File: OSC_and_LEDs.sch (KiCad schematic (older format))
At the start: 56 parts, among them Q11 IRLML2502, Q12 IRLML2502, Q14 IRLML2502, Q15 IRLML2502, Q8 IRLML2502, Q9 IRLML2502, U1 xc7a50tftg256, X1 ASFLMB

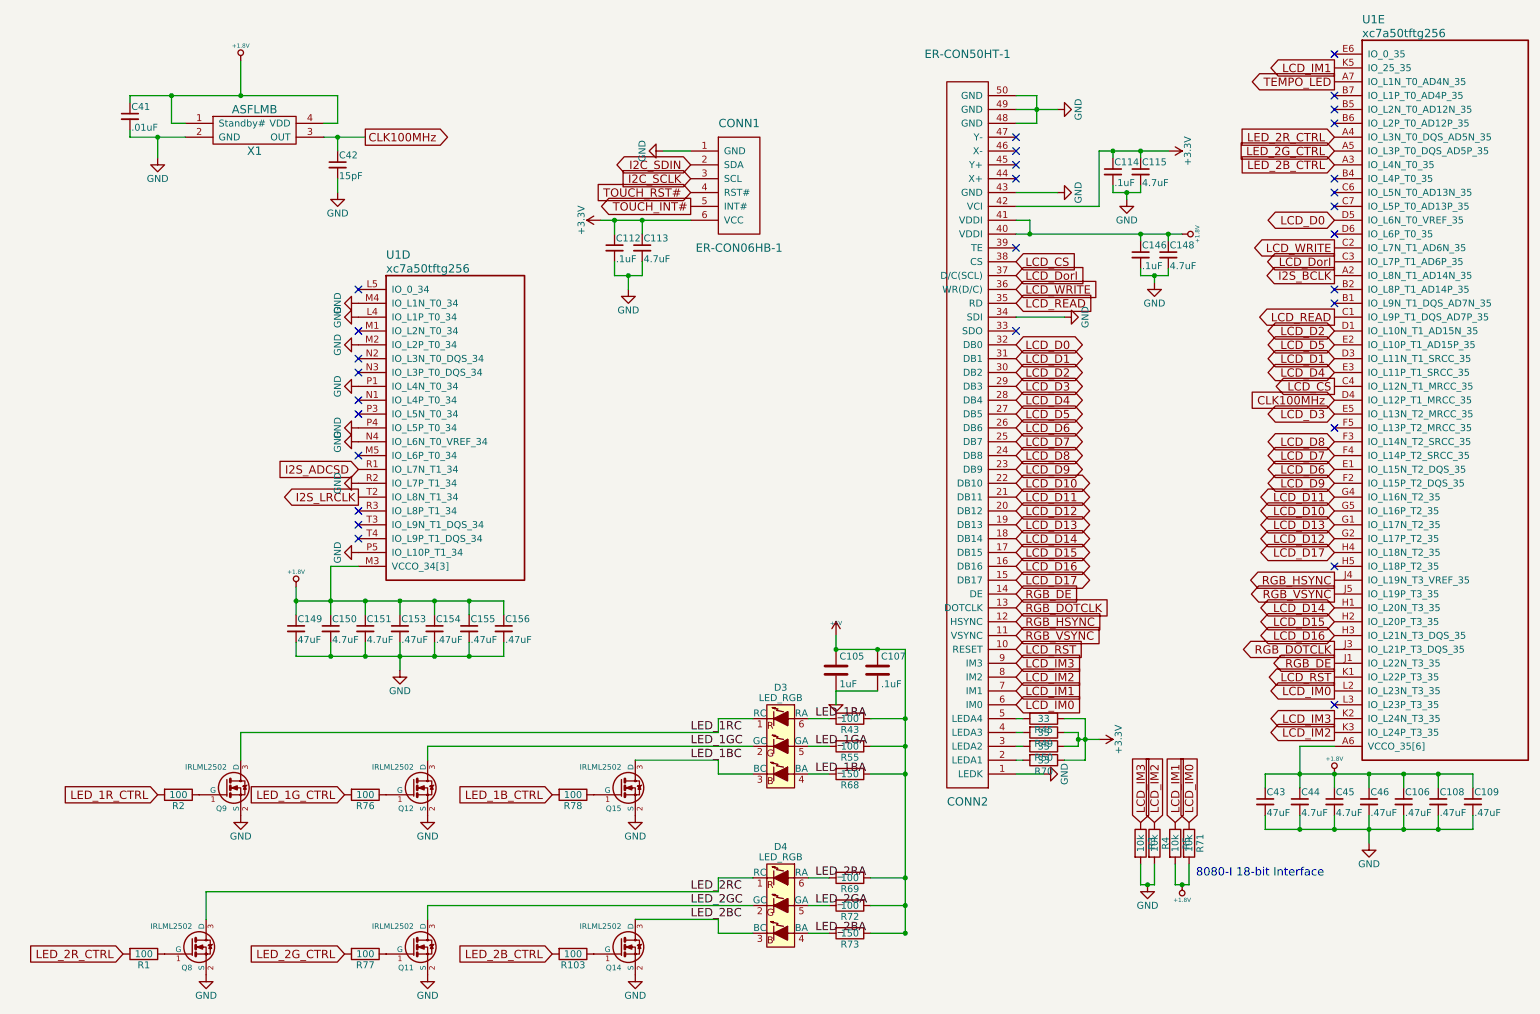
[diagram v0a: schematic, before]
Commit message: added and length-matched DDR2 ram, compliant to Xilinx MIG
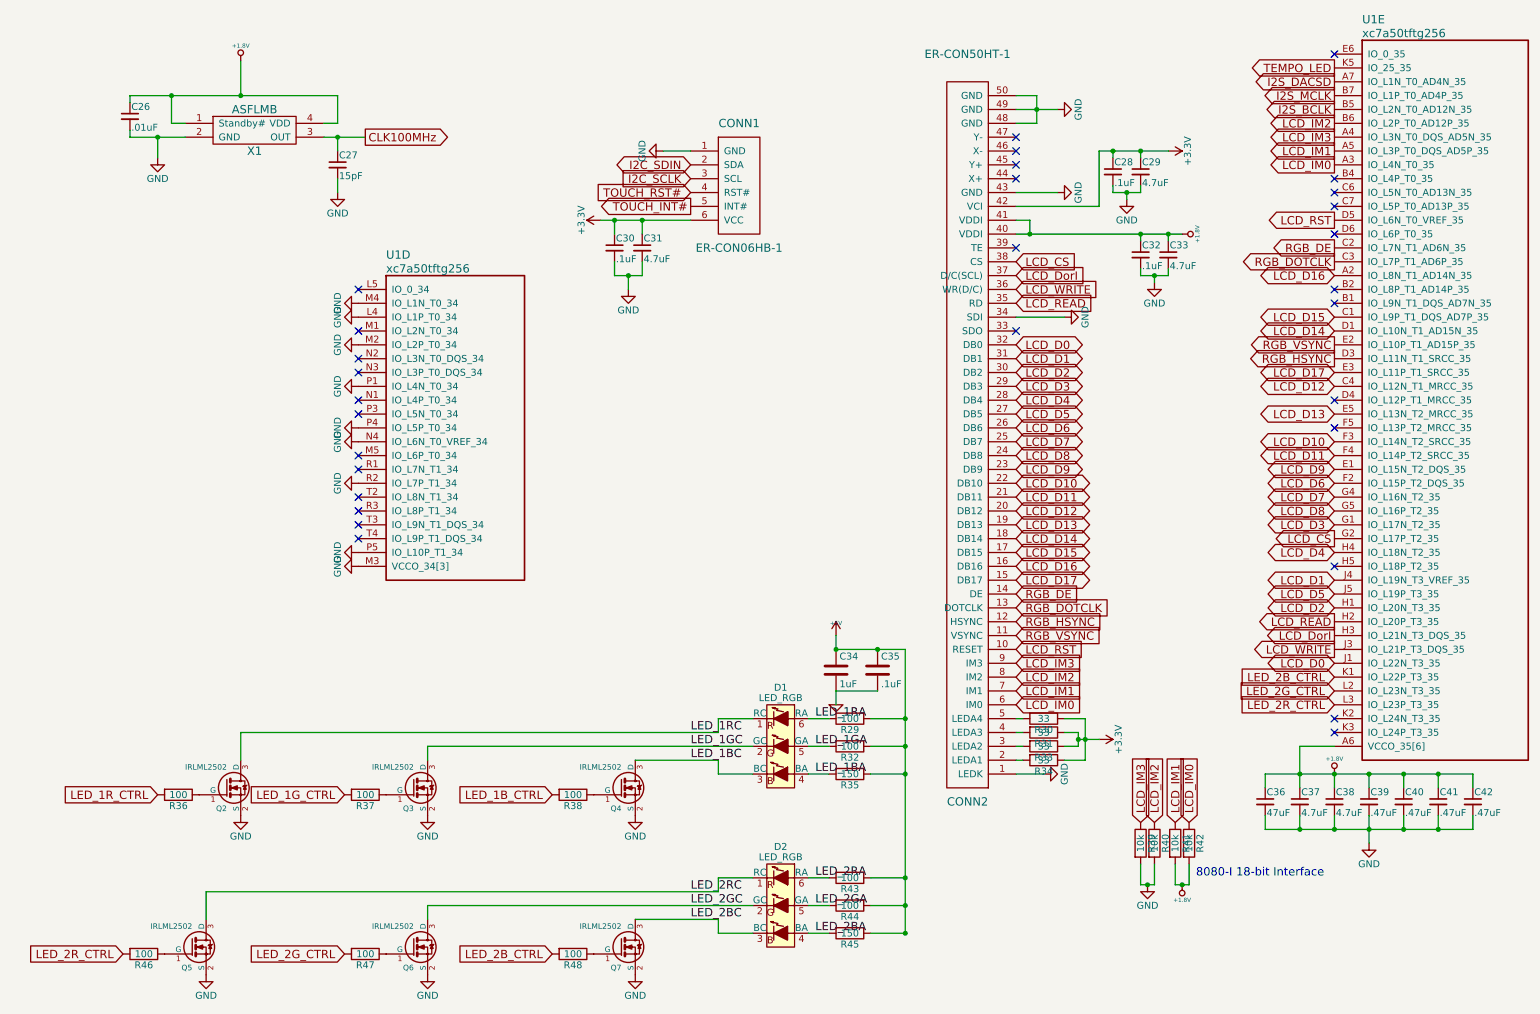
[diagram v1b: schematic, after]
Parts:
- removed C149: 47uF, Capacitors_SMD:C_1210, symbol C_Small
- removed C150, C151: 4.7uF, Capacitors_SMD:C_0805, symbol C_Small
- removed C153, C154, C155, C156: .47uF, Capacitors_SMD:C_0603, symbol C_Small
- renumbered C41 to C26, C42 to C27, C114 to C28, C115 to C29, C112 to C30, C113 to C31, C146 to C32, C148 to C33, C105 to C34, C107 to C35, C43 to C36, C44 to C37, C45 to C38, C46 to C39, C106 to C40, C108 to C41, C109 to C42, D3 to D1, D4 to D2, Q9 to Q2, Q12 to Q3, Q15 to Q4, Q8 to Q5, Q11 to Q6, Q14 to Q7, R43 to R29, R45 to R30, R49 to R31, R55 to R32, R50 to R33, R70 to R34, R68 to R35, R2 to R36, R76 to R37, R78 to R38, R3 to R39, R4 to R40, R5 to R41, R71 to R42, R69 to R43, R72 to R44, R73 to R45, R1 to R46, R77 to R47, R103 to R48
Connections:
- net +1.8V: no longer U1.M3 (VCCO_34[3]), U1.R4 (VCCO_34[3]), U1.T1 (VCCO_34[3])
- net CLK100MHz: no longer U1.D4 (IO_L12P_T1_MRCC_35)
- net GND: now also U1.M3 (VCCO_34[3]), U1.R4 (VCCO_34[3]), U1.T1 (VCCO_34[3])
- net I2S_BCLK: now also U1.B5 (IO_L2N_T0_AD12N_35); no longer U1.A2 (IO_L8N_T1_AD14N_35)
- net LCD_CS: now also U1.G2 (IO_L17P_T2_35); no longer U1.C4 (IO_L12N_T1_MRCC_35)
- net LCD_D0: now also U1.J1 (IO_L22N_T3_35); no longer U1.D5 (IO_L6N_T0_VREF_35)
- net LCD_D1: now also U1.J4 (IO_L19N_T3_VREF_35); no longer U1.D3 (IO_L11N_T1_SRCC_35)
- net LCD_D10: now also U1.F3 (IO_L14N_T2_SRCC_35); no longer U1.G5 (IO_L16P_T2_35)
- net LCD_D11: now also U1.F4 (IO_L14P_T2_SRCC_35); no longer U1.G4 (IO_L16N_T2_35)
- net LCD_D12: now also U1.C4 (IO_L12N_T1_MRCC_35); no longer U1.G2 (IO_L17P_T2_35)
- net LCD_D13: now also U1.E5 (IO_L13N_T2_MRCC_35); no longer U1.G1 (IO_L17N_T2_35)
- net LCD_D14: now also U1.D1 (IO_L10N_T1_AD15N_35); no longer U1.H1 (IO_L20N_T3_35)
- net LCD_D15: now also U1.C1 (IO_L9P_T1_DQS_AD7P_35); no longer U1.H2 (IO_L20P_T3_35)
- net LCD_D16: now also U1.A2 (IO_L8N_T1_AD14N_35); no longer U1.H3 (IO_L21N_T3_DQS_35)
- net LCD_D17: now also U1.E3 (IO_L11P_T1_SRCC_35); no longer U1.H4 (IO_L18N_T2_35)
- net LCD_D2: now also U1.H1 (IO_L20N_T3_35); no longer U1.D1 (IO_L10N_T1_AD15N_35)
- net LCD_D3: now also U1.G1 (IO_L17N_T2_35); no longer U1.E5 (IO_L13N_T2_MRCC_35)
- net LCD_D4: now also U1.H4 (IO_L18N_T2_35); no longer U1.E3 (IO_L11P_T1_SRCC_35)
- net LCD_D5: now also U1.J5 (IO_L19P_T3_35); no longer U1.E2 (IO_L10P_T1_AD15P_35)
- net LCD_D6: now also U1.F2 (IO_L15P_T2_DQS_35); no longer U1.E1 (IO_L15N_T2_DQS_35)
- net LCD_D7: now also U1.G4 (IO_L16N_T2_35); no longer U1.F4 (IO_L14P_T2_SRCC_35)
- net LCD_D8: now also U1.G5 (IO_L16P_T2_35); no longer U1.F3 (IO_L14N_T2_SRCC_35)
- net LCD_D9: now also U1.E1 (IO_L15N_T2_DQS_35); no longer U1.F2 (IO_L15P_T2_DQS_35)
- net LCD_DorI: now also U1.H3 (IO_L21N_T3_DQS_35); no longer U1.C3 (IO_L7P_T1_AD6P_35)
- net LCD_IM0: now also U1.A3 (IO_L4N_T0_35); no longer U1.L2 (IO_L23N_T3_35)
- net LCD_IM1: now also U1.A5 (IO_L3P_T0_DQS_AD5P_35); no longer U1.K5 (IO_25_35)
- net LCD_IM2: now also U1.B6 (IO_L2P_T0_AD12P_35); no longer U1.K3 (IO_L24P_T3_35)
- net LCD_IM3: now also U1.A4 (IO_L3N_T0_DQS_AD5N_35); no longer U1.K2 (IO_L24N_T3_35)
- net LCD_READ: now also U1.H2 (IO_L20P_T3_35); no longer U1.C1 (IO_L9P_T1_DQS_AD7P_35)
- net LCD_RST: now also U1.D5 (IO_L6N_T0_VREF_35); no longer U1.K1 (IO_L22P_T3_35)
- net LCD_WRITE: now also U1.J3 (IO_L21P_T3_DQS_35); no longer U1.C2 (IO_L7N_T1_AD6N_35)
- net LED_2B_CTRL: now also U1.K1 (IO_L22P_T3_35); no longer U1.A3 (IO_L4N_T0_35)
- net LED_2G_CTRL: now also U1.L2 (IO_L23N_T3_35); no longer U1.A5 (IO_L3P_T0_DQS_AD5P_35)
- net LED_2R_CTRL: now also U1.L3 (IO_L23P_T3_35); no longer U1.A4 (IO_L3N_T0_DQS_AD5N_35)
- net RGB_DE: now also U1.C2 (IO_L7N_T1_AD6N_35); no longer U1.J1 (IO_L22N_T3_35)
- net RGB_DOTCLK: now also U1.C3 (IO_L7P_T1_AD6P_35); no longer U1.J3 (IO_L21P_T3_DQS_35)
- net RGB_HSYNC: now also U1.D3 (IO_L11N_T1_SRCC_35); no longer U1.J4 (IO_L19N_T3_VREF_35)
- net RGB_VSYNC: now also U1.E2 (IO_L10P_T1_AD15P_35); no longer U1.J5 (IO_L19P_T3_35)
- net TEMPO_LED: now also U1.K5 (IO_25_35); no longer U1.A7 (IO_L1N_T0_AD4N_35)
- net I2S_MCLK: now reaches U1.B7 (IO_L1P_T0_AD4P_35)
- net I2S_ADCSD: no longer names the net of U1.R1 (IO_L7N_T1_34)
- net I2S_LRCLK: no longer names the net of U1.T2 (IO_L8N_T1_34)
- new net I2S_DACSD: U1.A7 (IO_L1N_T0_AD4N_35)
- no-connect marks 29 -> 30
